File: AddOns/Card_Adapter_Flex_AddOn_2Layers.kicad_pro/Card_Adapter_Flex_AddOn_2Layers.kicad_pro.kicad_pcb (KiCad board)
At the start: 2 copper layers, 57.4 x 27 mm, 28 parts, among them J1 17-pin-FPC, J2 4-pin-FPC, U1 5PB1214CMGK8, U3 5PB1214CMGK8

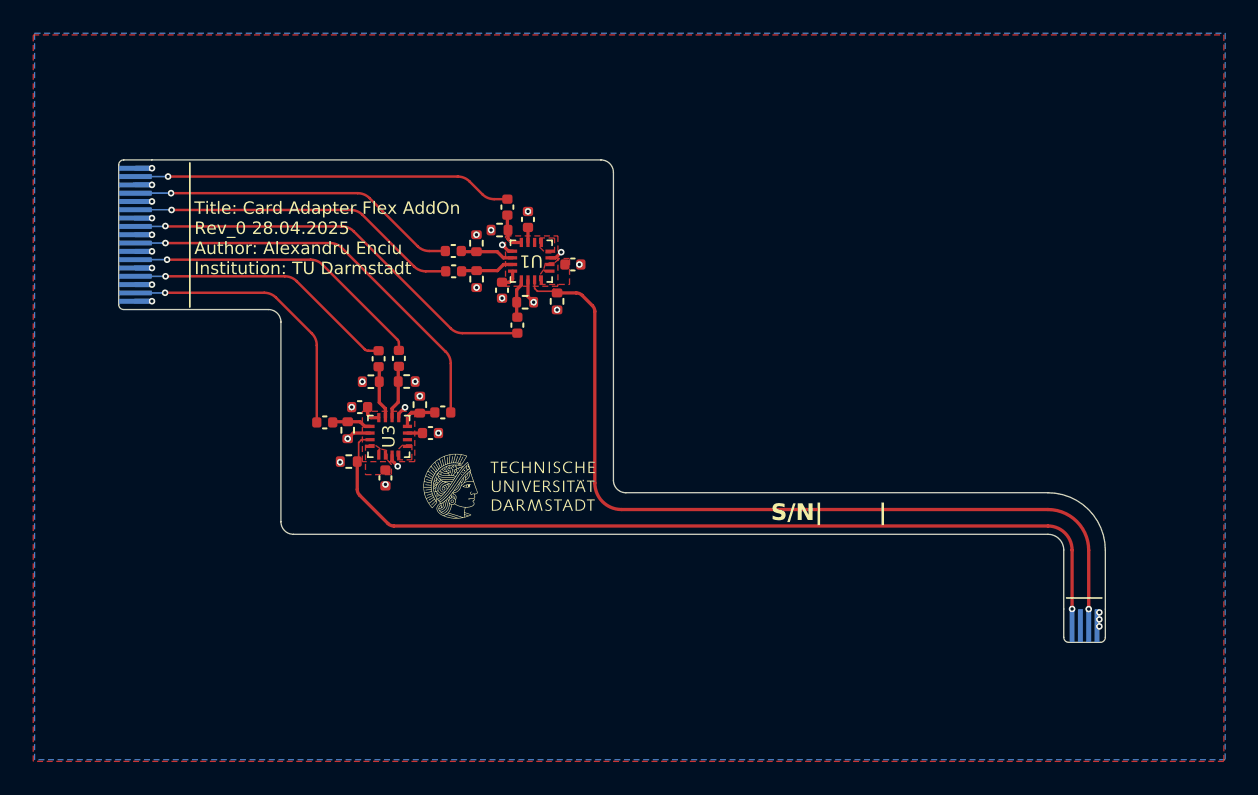
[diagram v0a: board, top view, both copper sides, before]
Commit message: Update PCB layout and net assignments for new capacitors
Added new nets and updated net assignments for several capacitors (C11, C12, C13, C14, C18, C19, C20, C21) in the PCB layout. Modified footprints, positions, and values for various components including resistors and capacitors. Updated backup files and added a lock file for the project.
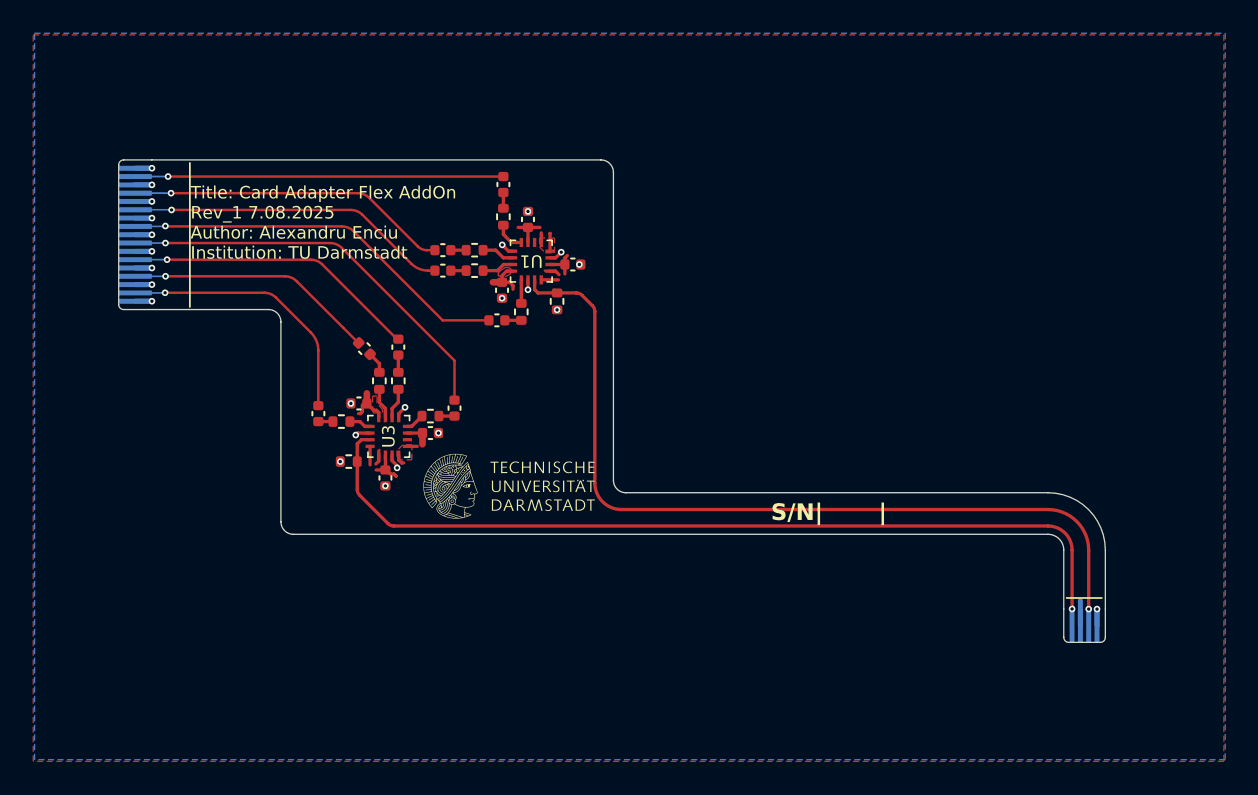
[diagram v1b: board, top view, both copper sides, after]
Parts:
- R1, R13, R14, R15, R16, R2, R3, R4: value 50 -> 33
- U1, U3: value 5PB1214CMGK8 -> 5PB1214
- moved C14 1.38 mm to (86.2, 53.9)
- moved C11 1.26 mm to (85.8, 62.1), turned to 0 degrees
- moved C19 1.05 mm to (77.9, 63.8), turned to -45 degrees
- moved R13 0.94 mm to (81.9, 67.9), turned to 180 degrees
- moved R1 0.83 mm to (86.2, 55.9), turned to -90 degrees
- moved C21 0.75 mm to (83.3, 67.4), turned to -90 degrees
- moved C20 0.68 mm to (79.9, 63.7)
- moved C18 0.66 mm to (75.1, 67.7), turned to -90 degrees
- moved C12 0.65 mm to (82.6, 59.1)
- moved R16 0.64 mm to (76.5, 68.2), turned to 0 degrees
- moved C13 0.63 mm to (82.6, 57.9)
- moved R4 0.62 mm to (87.3, 61.6), turned to 90 degrees
- moved R3 0.52 mm to (84.5, 59.1), turned to 0 degrees
- moved R15 0.52 mm to (78.8, 65.7), turned to -90 degrees
- moved R14 0.51 mm to (79.9, 65.7), turned to -90 degrees
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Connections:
- C11 pad 2: Net-(U1-CLK_OUT1) -> Net-(C11-Pad2)
- C12 pad 2: Net-(U1-CLK_OUT2) -> Net-(C12-Pad2)
- C13 pad 2: Net-(U1-CLK_OUT3) -> Net-(C13-Pad2)
- C14 pad 2: Net-(U1-CLK_OUT4) -> Net-(C14-Pad2)
- C18 pad 2: Net-(U3-CLK_OUT1) -> Net-(C18-Pad2)
- C19 pad 2: Net-(U3-CLK_OUT2) -> Net-(C19-Pad2)
- C20 pad 2: Net-(U3-CLK_OUT3) -> Net-(C20-Pad2)
- C21 pad 2: Net-(U3-CLK_OUT4) -> Net-(C21-Pad2)
- R1 pad 1: GND -> Net-(C14-Pad2)
- R13 pad 1: GND -> Net-(C21-Pad2)
- R14 pad 1: GND -> Net-(C20-Pad2)
- R15 pad 1: GND -> Net-(C19-Pad2)
- R16 pad 1: GND -> Net-(C18-Pad2)
- R2 pad 1: GND -> Net-(C13-Pad2)
- R3 pad 1: GND -> Net-(C12-Pad2)
- R4 pad 1: GND -> Net-(C11-Pad2)
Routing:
- net +3V3: track 4.19 -> 21.0 mm, vias 3 -> 1
- net Heim_time_out_1: track 25.6 -> 23.6 mm
- net Net-(U3-CLK_OUT3): track 3.25 -> 1.86 mm
- net Net-(U3-CLK_OUT2): track 3.23 -> 1.86 mm
- net Master_trigger_out_2: track 16.4 -> 15.1 mm
- net Net-(C19-Pad2): track 0.00 -> 1.32 mm
- net Net-(U1-CLK_OUT2): track 3.23 -> 1.93 mm
- net Net-(U1-CLK_OUT3): track 3.25 -> 1.97 mm
- net Net-(U3-CLK_OUT4): track 2.34 -> 1.13 mm
- net Net-(U3-CLK_OUT1): track 2.38 -> 1.33 mm
- net Net-(C20-Pad2): track 0.00 -> 1.04 mm
- net Master_trigger_out_1: track 17.0 -> 16.0 mm
- net Net-(C11-Pad2): track 0.00 -> 0.99 mm
- net Net-(U1-CLK_OUT1): track 2.38 -> 1.41 mm
- net Net-(C14-Pad2): track 0.00 -> 0.95 mm
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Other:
- board text added: "Title: Card Adapter Flex AddOn Rev_1 7.08.2025 Author: Alexandru Enciu Institution: TU Darmstadt"
- board text removed: "Title: Card Adapter Flex AddOn Rev_0 28.04.2025 Author: Alexandru Enciu Institution: TU Darmstadt"

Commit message: .
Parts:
- R11, R12: value 50 -> 10k
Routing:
- net +3V3: track 21.0 -> 24.3 mm
